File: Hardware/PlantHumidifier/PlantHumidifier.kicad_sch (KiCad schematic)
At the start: 9 parts

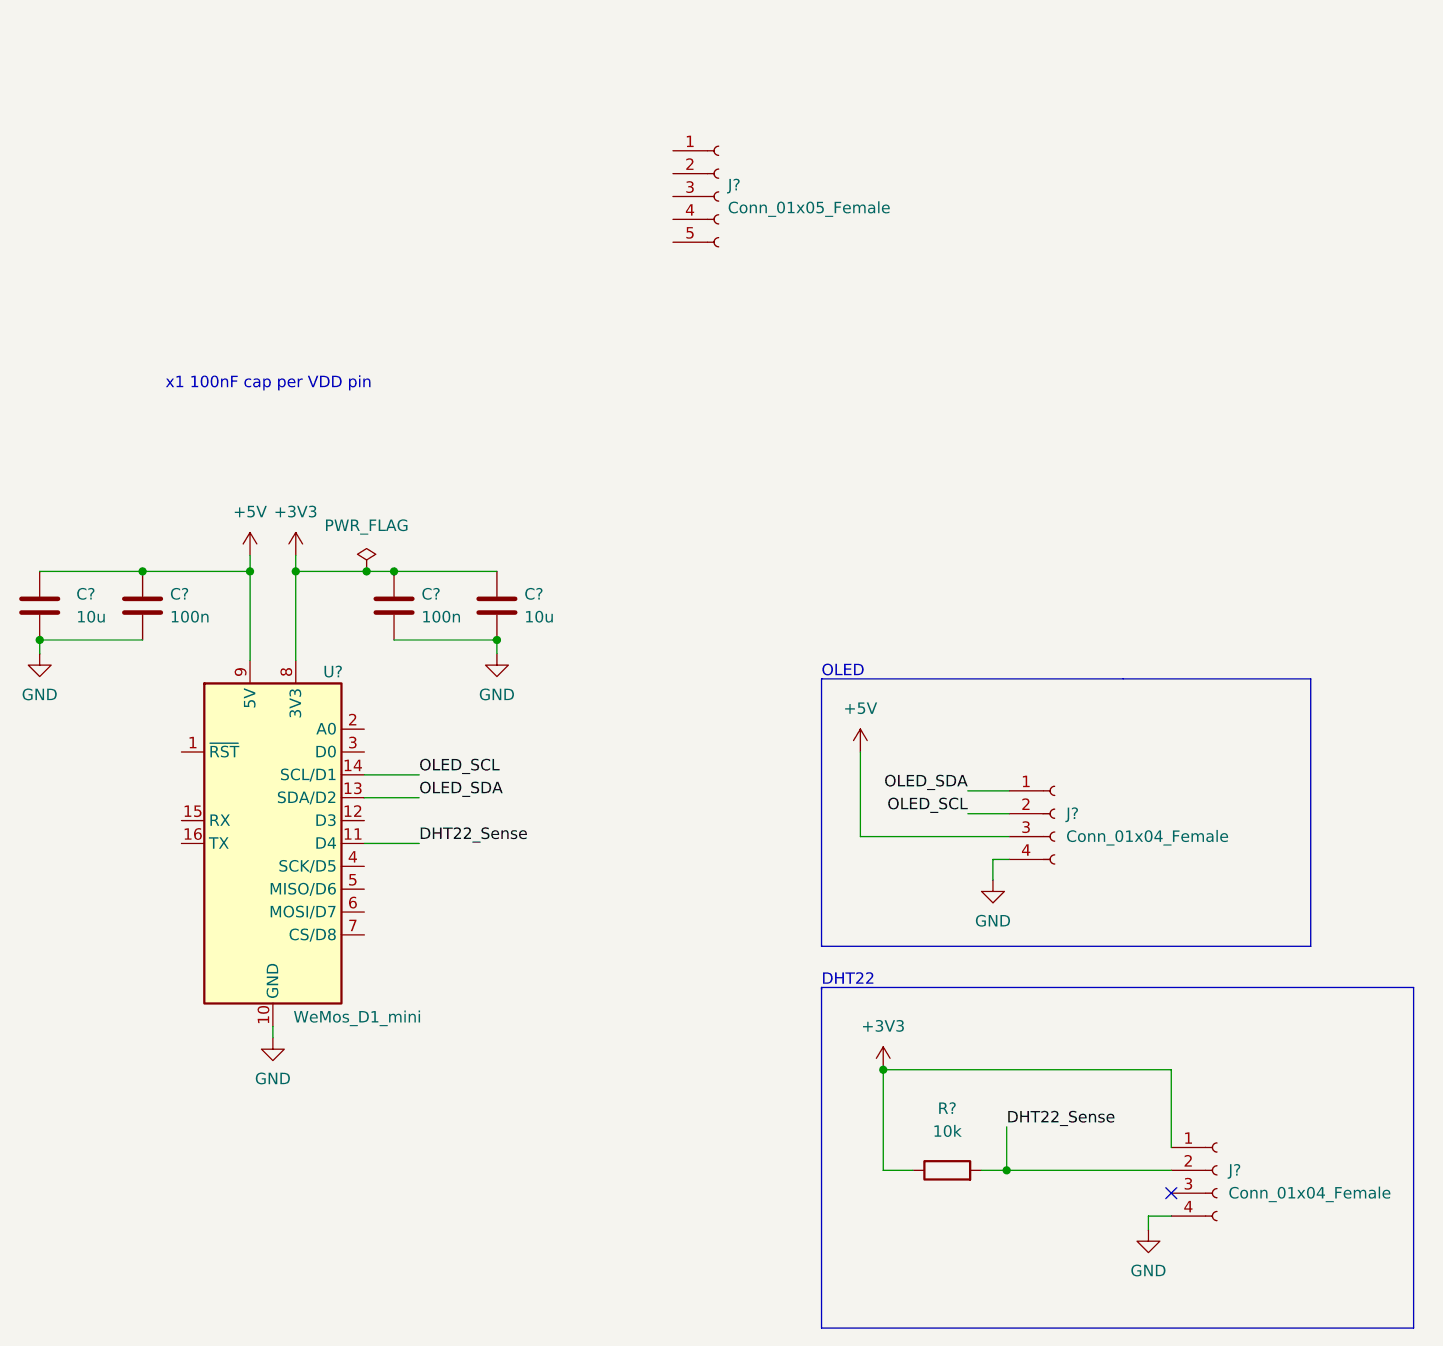
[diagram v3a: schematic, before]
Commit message: Schematic: Finish wiring rotary encoder with momentary switch
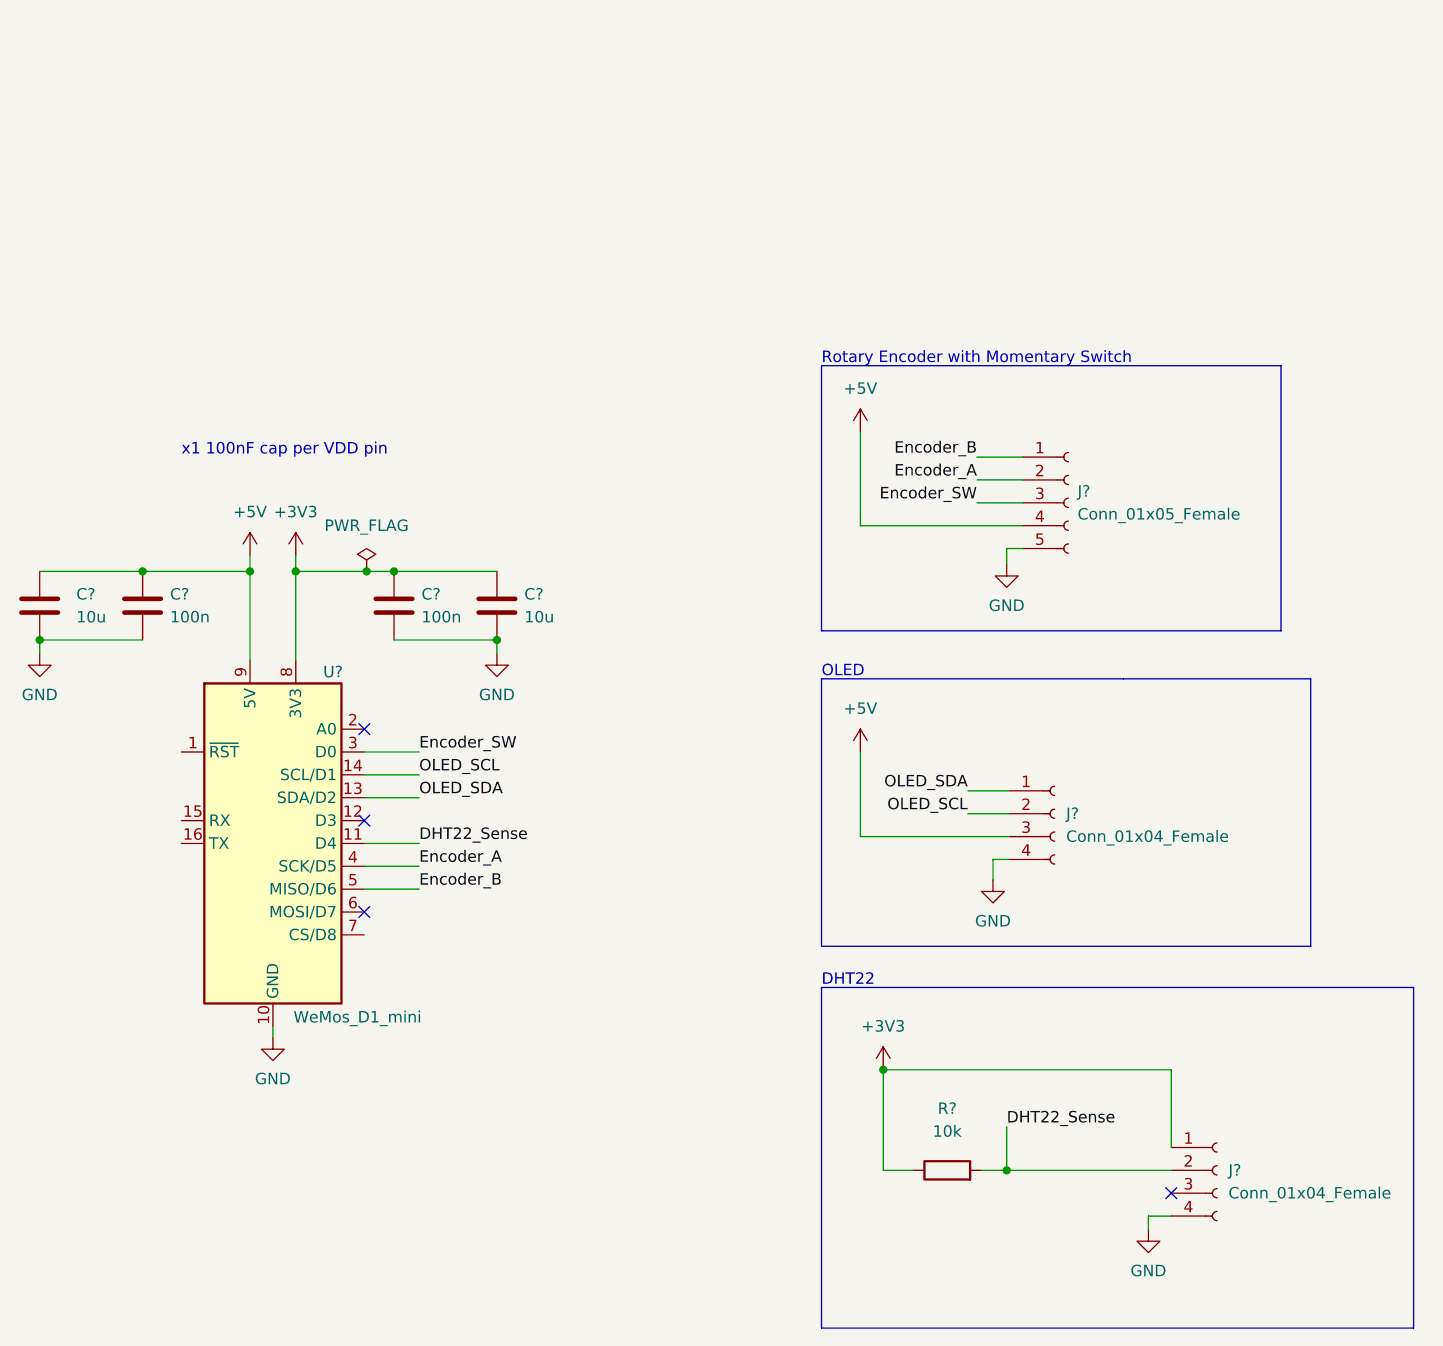
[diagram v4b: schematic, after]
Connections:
- net +5V: now also J?.4 (Pin_4)
- net GND: now also J?.5 (Pin_5)
- net Encoder_B: now reaches J?.1 (Pin_1)
- net Encoder_B: now also U?.5 (MISO/D6)
- net Encoder_A: now reaches J?.2 (Pin_2)
- net Encoder_A: now also U?.4 (SCK/D5)
- net Encoder_SW: now reaches J?.3 (Pin_3)
- net Encoder_SW: now also U?.3 (D0)
- no-connect marks 1 -> 4
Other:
- note added: "Rotary Encoder with Momentary Switch"
- moved on the sheet: J?
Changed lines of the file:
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@@
   (junction (at 164.592 77.724) (diameter 0) (color 0 0 0 0)
   )
+  (no_connect (at 161.29 105.41))
   (no_connect (at 250.952 146.812))
+  (no_connect (at 161.29 115.57))
+  (no_connect (at 161.29 95.25))
   (wire (pts (xy 148.59 75.946) (xy 148.59 77.724))
     (stroke (width 0) (type default) (color 0 0 0 0))
@@
     (stroke (width 0) (type default) (color 0 0 0 0))
   )
+  (wire (pts (xy 161.29 97.79) (xy 167.386 97.79))
+    (stroke (width 0) (type default) (color 0 0 0 0))
+  )
   (polyline (pts (xy 212.09 123.952) (xy 277.876 123.952))
     (stroke (width 0) (type default) (color 0 0 0 0))
@@
     (stroke (width 0) (type default) (color 0 0 0 0))
   )
+  (wire (pts (xy 161.29 110.49) (xy 167.386 110.49))
+    (stroke (width 0) (type default) (color 0 0 0 0))
+  )
   (wire (pts (xy 218.948 133.096) (xy 218.948 144.272))
     (stroke (width 0) (type default) (color 0 0 0 0))
@@
     (stroke (width 0) (type default) (color 0 0 0 0))
   )
+  (wire (pts (xy 229.362 70.104) (xy 234.442 70.104))
+    (stroke (width 0) (type default) (color 0 0 0 0))
+  )
   (wire (pts (xy 148.59 77.724) (xy 148.59 87.63))
     (stroke (width 0) (type default) (color 0 0 0 0))
@@
     (stroke (width 0) (type default) (color 0 0 0 0))
   )
+  (wire (pts (xy 216.408 72.644) (xy 234.442 72.644))
+    (stroke (width 0) (type default) (color 0 0 0 0))
+  )
   (wire (pts (xy 229.87 144.272) (xy 232.664 144.272))
     (stroke (width 0) (type default) (color 0 0 0 0))
@@
     (stroke (width 0) (type default) (color 0 0 0 0))
   )
+  (polyline (pts (xy 212.09 84.328) (xy 263.144 84.328))
+    (stroke (width 0) (type default) (color 0 0 0 0))
+  )
   (wire (pts (xy 153.67 75.946) (xy 153.67 77.724))
     (stroke (width 0) (type default) (color 0 0 0 0))
   )
+  (wire (pts (xy 161.29 113.03) (xy 167.386 113.03))
+    (stroke (width 0) (type default) (color 0 0 0 0))
+  )
   (polyline (pts (xy 245.618 89.662) (xy 212.09 89.662))
     (stroke (width 0) (type default) (color 0 0 0 0))
@@
     (stroke (width 0) (type default) (color 0 0 0 0))
   )
+  (polyline (pts (xy 263.144 54.864) (xy 212.09 54.864))
+    (stroke (width 0) (type default) (color 0 0 0 0))
+  )
   (polyline (pts (xy 245.618 89.662) (xy 266.446 89.662))
     (stroke (width 0) (type default) (color 0 0 0 0))
   )
+  (wire (pts (xy 232.664 75.184) (xy 234.442 75.184))
+    (stroke (width 0) (type default) (color 0 0 0 0))
+  )
   (wire (pts (xy 125.222 77.724) (xy 136.652 77.724))
     (stroke (width 0) (type default) (color 0 0 0 0))
@@
     (stroke (width 0) (type default) (color 0 0 0 0))
   )
+  (polyline (pts (xy 263.144 84.328) (xy 263.144 54.864))
+    (stroke (width 0) (type default) (color 0 0 0 0))
+  )
   (wire (pts (xy 148.59 77.724) (xy 136.652 77.724))
     (stroke (width 0) (type default) (color 0 0 0 0))
   )
+  (wire (pts (xy 229.362 67.564) (xy 234.442 67.564))
+    (stroke (width 0) (type default) (color 0 0 0 0))
+  )
+  (wire (pts (xy 229.362 65.024) (xy 234.442 65.024))
+    (stroke (width 0) (type default) (color 0 0 0 0))
+  )
   (wire (pts (xy 161.29 102.87) (xy 167.386 102.87))
     (stroke (width 0) (type default) (color 0 0 0 0))
@@
     (stroke (width 0) (type default) (color 0 0 0 0))
   )
+  (wire (pts (xy 232.664 76.962) (xy 232.664 75.184))
+    (stroke (width 0) (type default) (color 0 0 0 0))
+  )
   (wire (pts (xy 232.664 139.446) (xy 232.664 144.272))
     (stroke (width 0) (type default) (color 0 0 0 0))
   )
+  (polyline (pts (xy 212.09 54.864) (xy 212.09 84.328))
+    (stroke (width 0) (type default) (color 0 0 0 0))
+  )
+  (wire (pts (xy 216.408 62.23) (xy 216.408 72.644))
+    (stroke (width 0) (type default) (color 0 0 0 0))
+  )
   (wire (pts (xy 161.29 100.33) (xy 167.386 100.33))
     (stroke (width 0) (type default) (color 0 0 0 0))
   )
-  (text "x1 100nF cap per VDD pin" (at 139.192 57.658 0)
+  (text "x1 100nF cap per VDD pin" (at 140.97 65.024 0)
+    (effects (font (size 1.27 1.27)) (justify left bottom))
+  )
+  (text "Rotary Encoder with Momentary Switch" (at 212.09 54.864 0)
     (effects (font (size 1.27 1.27)) (justify left bottom))
   )
@@
   (label "DHT22_Sense" (at 167.386 107.95 0)
     (effects (font (size 1.27 1.27)) (justify left bottom))
+  )
+  (label "Encoder_A" (at 229.362 67.564 180)
+    (effects (font (size 1.27 1.27)) (justify right bottom))
+  )
+  (label "Encoder_B" (at 229.362 65.024 180)
+    (effects (font (size 1.27 1.27)) (justify right bottom))
   )
   (label "OLED_SCL" (at 167.386 100.33 0)
@@
     (effects (font (size 1.27 1.27)) (justify left bottom))
   )
+  (label "Encoder_SW" (at 229.362 70.104 180)
+    (effects (font (size 1.27 1.27)) (justify right bottom))
+  )
   (label "OLED_SDA" (at 228.346 102.108 180)
     (effects (font (size 1.27 1.27)) (justify right bottom))
+  )
+  (label "Encoder_SW" (at 167.386 97.79 0)
+    (effects (font (size 1.27 1.27)) (justify left bottom))
+  )
+  (label "Encoder_A" (at 167.386 110.49 0)
+    (effects (font (size 1.27 1.27)) (justify left bottom))
+  )
+  (label "Encoder_B" (at 167.386 113.03 0)
+    (effects (font (size 1.27 1.27)) (justify left bottom))
   )
   (symbol (lib_id "Device:C") (at 164.592 81.534 0) (unit 1)
@@
     (pin "2")
   )
+  (symbol (lib_id "power:GND") (at 232.664 76.962 0) (unit 1)
+    (in_bom yes) (on_board yes) (fields_autoplaced)
+    (property "Reference" "#PWR?" (id 0) (at 232.664 83.312 0)
+      (effects (font (size 1.27 1.27)) hide)
+    )
+    (property "Value" "GND" (id 1) (at 232.664 81.534 0))
+    (property "Footprint" "" (id 2) (at 232.664 76.962 0)
+      (effects (font (size 1.27 1.27)) hide)
+    )
+    (property "Datasheet" "" (id 3) (at 232.664 76.962 0)
+      (effects (font (size 1.27 1.27)) hide)
+    )
+    (pin "1")
+  )
   (symbol (lib_id "power:GND") (at 125.222 86.868 0) (unit 1)
     (in_bom yes) (on_board yes) (fields_autoplaced)
@@
     )
     (property "Datasheet" "" (id 3) (at 153.67 75.946 0)
+      (effects (font (size 1.27 1.27)) hide)
+    )
+    (pin "1")
+  )
+  (symbol (lib_id "power:+5V") (at 216.408 62.23 0) (unit 1)
+    (in_bom yes) (on_board yes) (fields_autoplaced)
+    (property "Reference" "#PWR?" (id 0) (at 216.408 66.04 0)
+      (effects (font (size 1.27 1.27)) hide)
+    )
+    (property "Value" "+5V" (id 1) (at 216.408 57.404 0))
+    (property "Footprint" "" (id 2) (at 216.408 62.23 0)
+      (effects (font (size 1.27 1.27)) hide)
+    )
+    (property "Datasheet" "" (id 3) (at 216.408 62.23 0)
       (effects (font (size 1.27 1.27)) hide)
     )
@@
     (pin "2")
   )
-  (symbol (lib_id "Connector:Conn_01x05_Female") (at 200.66 36.068 0) (unit 1)
-    (in_bom yes) (on_board yes) (fields_autoplaced)
-    (property "Reference" "J?" (id 0) (at 201.676 34.7979 0)
-      (effects (font (size 1.27 1.27)) (justify left))
-    )
-    (property "Value" "Conn_01x05_Female" (id 1) (at 201.676 37.3379 0)
-      (effects (font (size 1.27 1.27)) (justify left))
-    )
-    (property "Footprint" "" (id 2) (at 200.66 36.068 0)
-      (effects (font (size 1.27 1.27)) hide)
-    )
-    (property "Datasheet" "~" (id 3) (at 200.66 36.068 0)
+  (symbol (lib_id "Connector:Conn_01x05_Female") (at 239.522 70.104 0) (unit 1)
+    (in_bom yes) (on_board yes) (fields_autoplaced)
+    (property "Reference" "J?" (id 0) (at 240.538 68.8339 0)
+      (effects (font (size 1.27 1.27)) (justify left))
+    )
+    (property "Value" "Conn_01x05_Female" (id 1) (at 240.538 71.3739 0)
+      (effects (font (size 1.27 1.27)) (justify left))
+    )
+    (property "Footprint" "" (id 2) (at 239.522 70.104 0)
+      (effects (font (size 1.27 1.27)) hide)
+    )
+    (property "Datasheet" "~" (id 3) (at 239.522 70.104 0)
       (effects (font (size 1.27 1.27)) hide)
     )
@@
       (reference "#PWR?") (unit 1) (value "GND") (footprint "")
     )
+    (path "/4f59d960-e3e5-4142-af04-748d258b5a1b"
+      (reference "#PWR?") (unit 1) (value "GND") (footprint "")
+    )
     (path "/4fd436a4-02d9-42ee-968a-9ab8efbc4f34"
       (reference "#PWR?") (unit 1) (value "GND") (footprint "")
@@
       (reference "#PWR?") (unit 1) (value "+3V3") (footprint "")
     )
+    (path "/55a410e5-ad86-4bfb-9e29-30b690ae6ba5"
+      (reference "#PWR?") (unit 1) (value "+5V") (footprint "")
+    )
     (path "/8848dd79-718c-4217-9cb5-0c12188193bc"
